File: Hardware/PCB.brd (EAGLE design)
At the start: 170.2 x 111.2 mm, 103 parts, among them IC1 BD5229G-TR, IC4 XC6220A331MR-G, J1 FH34SRJ-24S-0.5SH_99_, J2 SAMACSYS_PARTS_USB4110-GF-A, J3 QWIIC_RIGHT_ANGLE, J4 112A-TAAR-R03_ATTEND, Q1 20V/4.2A/52mΩ/1.4W, Q2 20V/4.2A/52mΩ/1.4W, Q3 SI1308EDL-T1-GE3, U1 W25Q512JVEIQ, U2 ESP32-C6-WROOM-1-N8, U3 DS3231SN#, U4 MAX17048G+T10

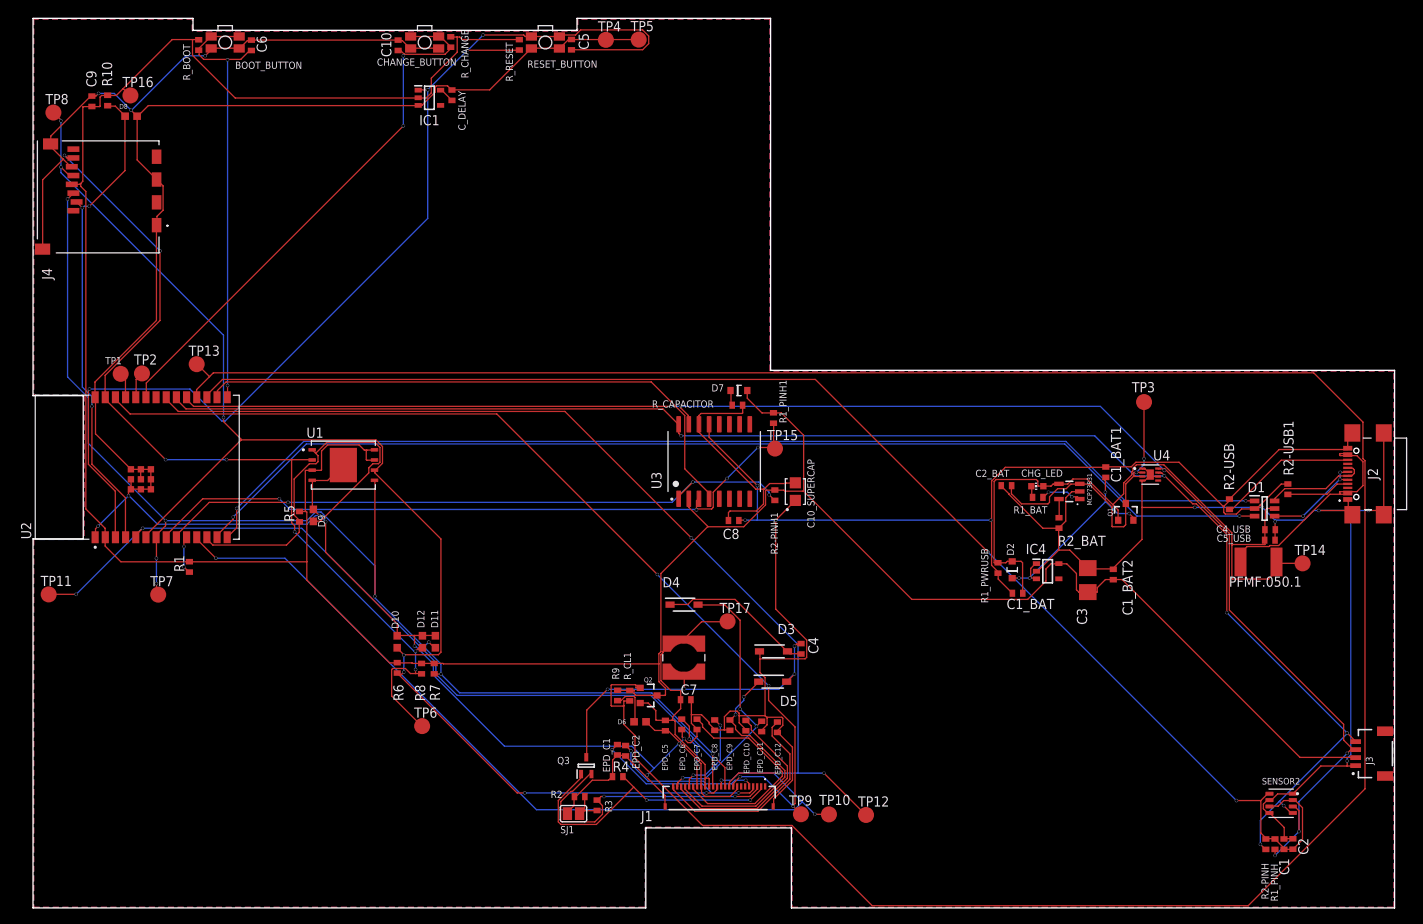
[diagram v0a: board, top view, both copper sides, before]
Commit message: Solved issues
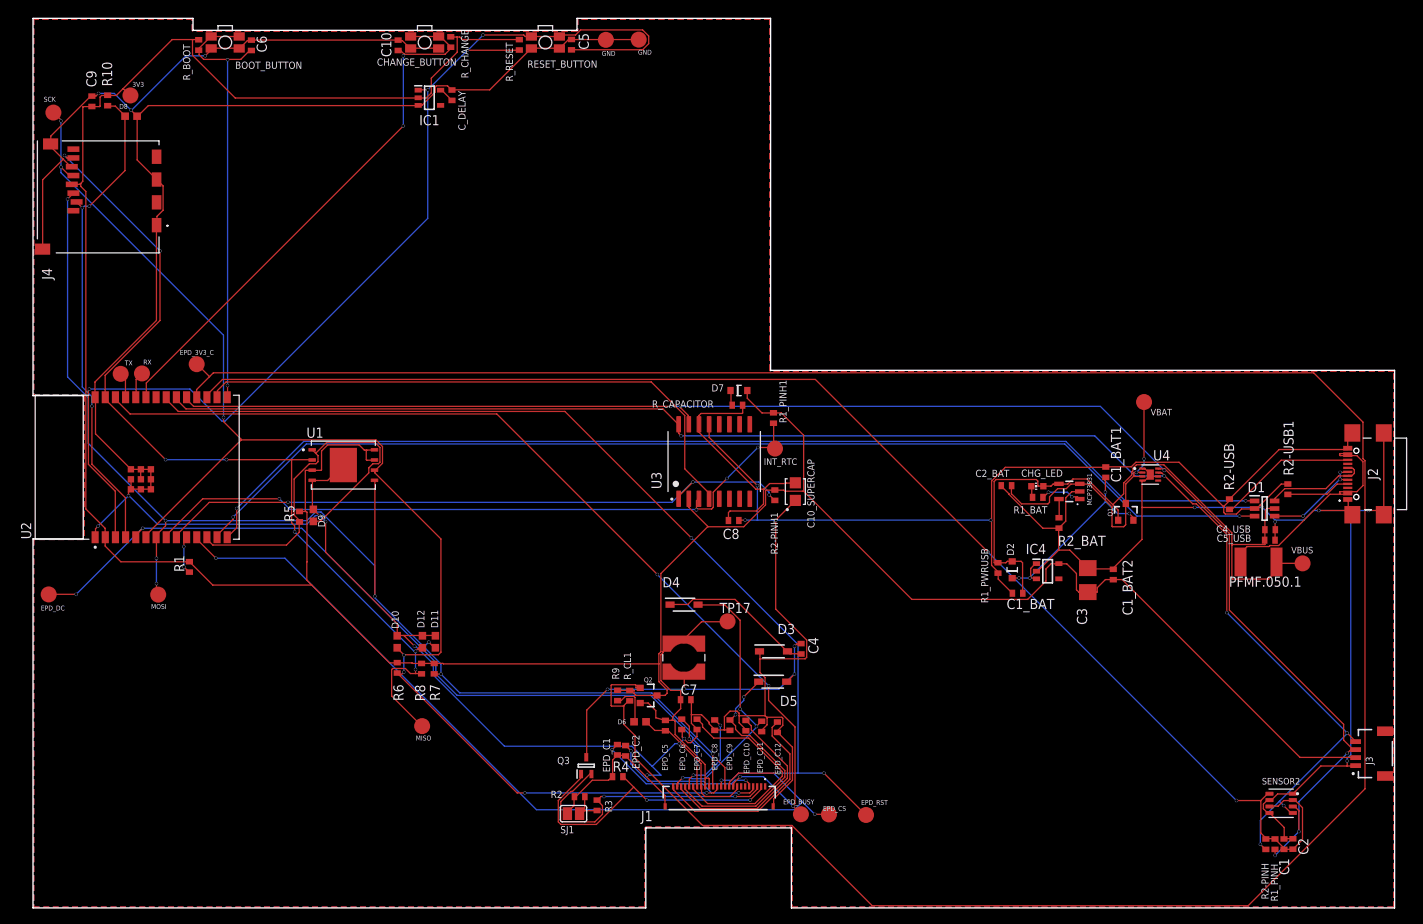
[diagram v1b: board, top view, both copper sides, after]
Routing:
- net GND: track 707.7 -> 710.2 mm
- net 3V3: track 388.6 -> 390.7 mm
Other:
- board text added: "3V3"
- board text added: "EPD_3V3_C"
- board text added: "EPD_BUSY"
- board text added: "EPD_CS"
- board text added: "EPD_DC"
- board text added: "EPD_RST"
- board text added: "GND"
- board text added: "INT_RTC"
- board text added: "MISO"
- board text added: "MOSI"
- board text added: "RX"
- board text added: "SCK"
- board text added: "TX"
- board text added: "VBAT"
- board text added: "VBUS"
